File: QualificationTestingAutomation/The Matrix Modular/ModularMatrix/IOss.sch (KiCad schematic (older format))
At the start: 10 parts, among them J1 Conn_02x32_Counter_Clockwise_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, J5 Conn_02x32_Counter_Clockwise_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, J6 Banana Jack, J7 Banana Jack, J8 Banana Jack, J9 Banana Jack

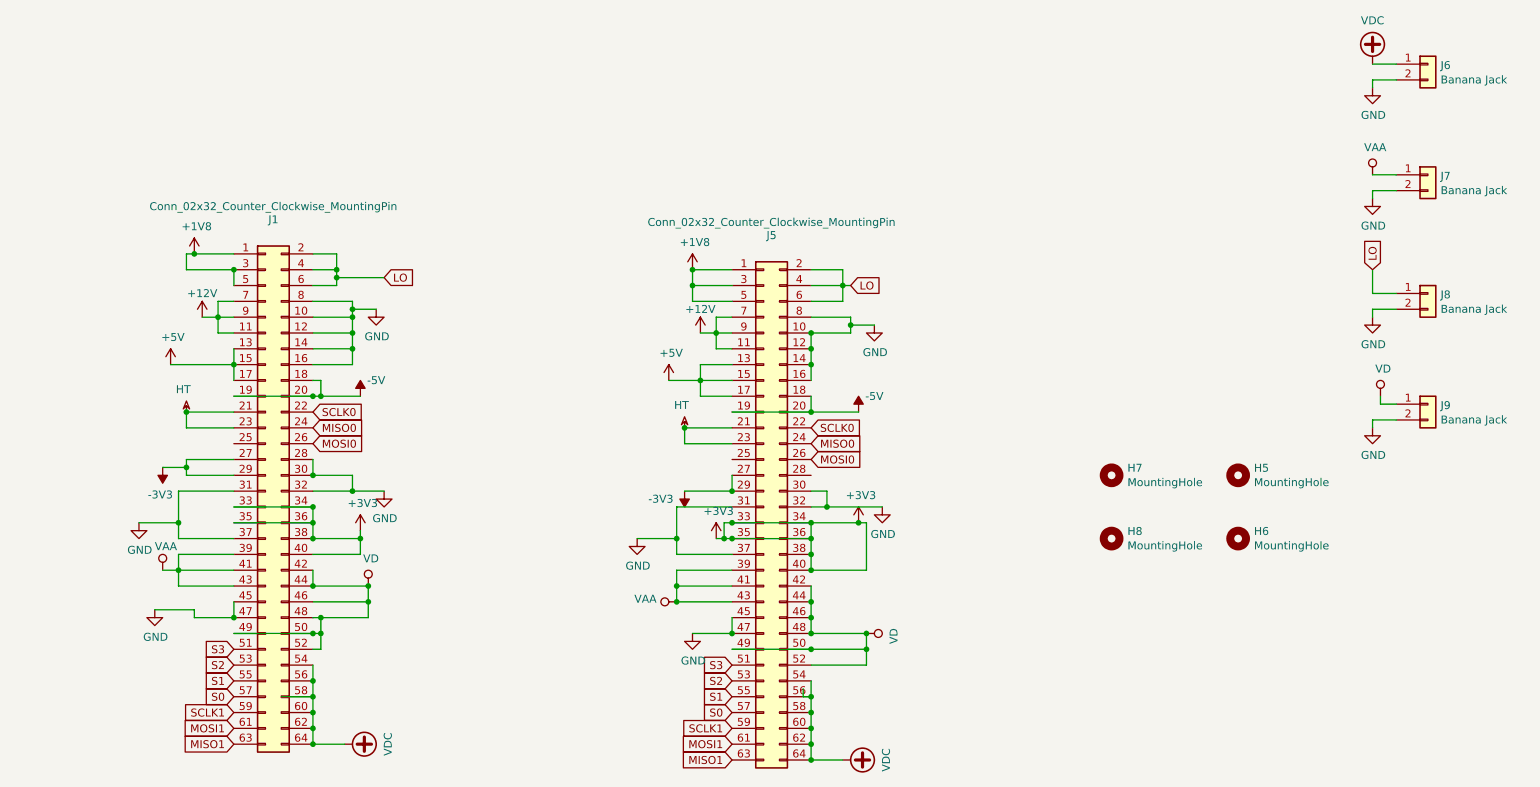
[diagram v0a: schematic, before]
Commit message: IO clean up added the 1v25 reference to Matrix Changed Some of the labels to more legible names.
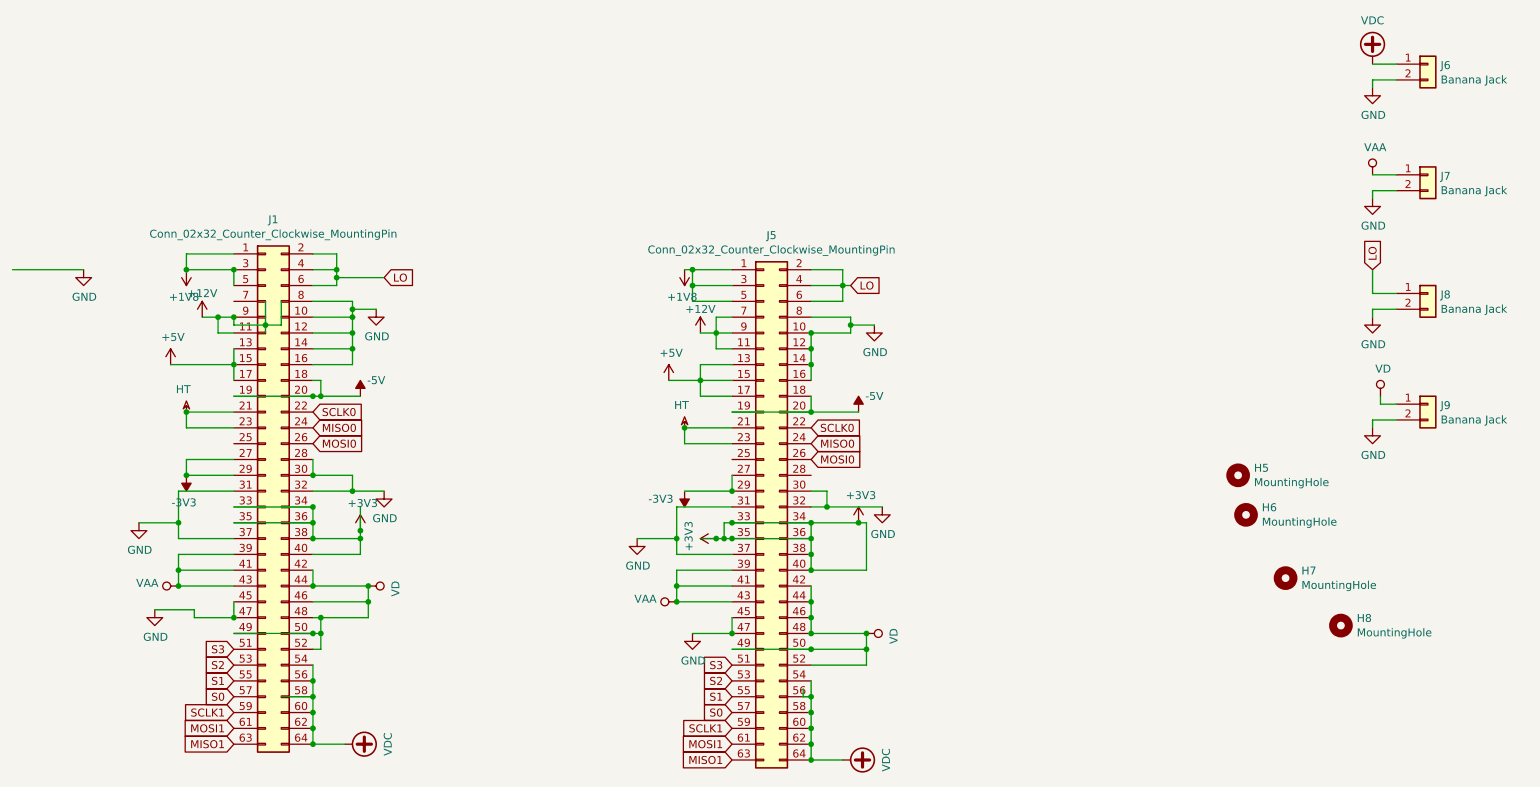
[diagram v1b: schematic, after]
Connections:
- wire segments 191 -> 195
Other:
- moved on the sheet: H6, H7, H8
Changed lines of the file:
@@
 L Mechanical:MountingHole H?
 U 1 1 5C9BCC1D
-P 9100 3900
+P 9150 3750
 AR Path="/5D942532/5C9BCC1D" Ref="H?"  Part="1"
 AR Path="/5D968A33/5C9BCC1D" Ref="H6"  Part="1"
-F 0 "H6" H 9200 3946 50  0000 L CNN
-F 1 "MountingHole" H 9200 3855 50  0000 L CNN
-F 2 "MountingHole:MountingHole_2.5mm" H 9100 3900 50  0001 C CNN
-F 3 "~" H 9100 3900 50  0001 C CNN
-	1    9100 3900
+F 0 "H6" H 9250 3796 50  0000 L CNN
+F 1 "MountingHole" H 9250 3705 50  0000 L CNN
+F 2 "MountingHole:MountingHole_2.5mm" H 9150 3750 50  0001 C CNN
+F 3 "~" H 9150 3750 50  0001 C CNN
+	1    9150 3750
 	1    0    0    -1
 $EndComp
@@
 L Mechanical:MountingHole H?
 U 1 1 5C9BCC1E
-P 8300 3500
+P 9400 4150
 AR Path="/5D942532/5C9BCC1E" Ref="H?"  Part="1"
 AR Path="/5D968A33/5C9BCC1E" Ref="H7"  Part="1"
-F 0 "H7" H 8400 3546 50  0000 L CNN
-F 1 "MountingHole" H 8400 3455 50  0000 L CNN
-F 2 "MountingHole:MountingHole_2.5mm" H 8300 3500 50  0001 C CNN
-F 3 "~" H 8300 3500 50  0001 C CNN
-	1    8300 3500
+F 0 "H7" H 9500 4196 50  0000 L CNN
+F 1 "MountingHole" H 9500 4105 50  0000 L CNN
+F 2 "MountingHole:MountingHole_2.5mm" H 9400 4150 50  0001 C CNN
+F 3 "~" H 9400 4150 50  0001 C CNN
+	1    9400 4150
 	1    0    0    -1
 $EndComp
@@
 L Mechanical:MountingHole H?
 U 1 1 5C9BCC1F
-P 8300 3900
+P 9750 4450
 AR Path="/5D942532/5C9BCC1F" Ref="H?"  Part="1"
 AR Path="/5D968A33/5C9BCC1F" Ref="H8"  Part="1"
-F 0 "H8" H 8400 3946 50  0000 L CNN
-F 1 "MountingHole" H 8400 3855 50  0000 L CNN
-F 2 "MountingHole:MountingHole_2.5mm" H 8300 3900 50  0001 C CNN
-F 3 "~" H 8300 3900 50  0001 C CNN
-	1    8300 3900
+F 0 "H8" H 9850 4496 50  0000 L CNN
+F 1 "MountingHole" H 9850 4405 50  0000 L CNN
+F 2 "MountingHole:MountingHole_2.5mm" H 9750 4450 50  0001 C CNN
+F 3 "~" H 9750 4450 50  0001 C CNN
+	1    9750 4450
 	1    0    0    -1
 $EndComp
@@
 L power:+1V8 #PWR?
 U 1 1 5DFE913D
-P 2500 2100
+P 2450 2200
 AR Path="/5D94288A/5DFE913D" Ref="#PWR?"  Part="1"
 AR Path="/5D968A33/5DFE913D" Ref="#PWR0169"  Part="1"
 AR Path="/5C90F517/5DFE913D" Ref="#PWR?"  Part="1"
-F 0 "#PWR0169" H 2500 1950 50  0001 C CNN
-F 1 "+1V8" H 2515 2273 50  0000 C CNN
-F 2 "" H 2500 2100 50  0001 C CNN
-F 3 "" H 2500 2100 50  0001 C CNN
-	1    2500 2100
-	1    0    0    -1
-$EndComp
+F 0 "#PWR0169" H 2450 2050 50  0001 C CNN
+F 1 "+1V8" H 2465 2373 50  0000 C CNN
+F 2 "" H 2450 2200 50  0001 C CNN
+F 3 "" H 2450 2200 50  0001 C CNN
+	1    2450 2200
+	-1   0    0    1
+$EndComp
+$Comp
+L power:GND #PWR0170
+U 1 1 5DFE914C
+P 1800 2200
+F 0 "#PWR0170" H 1800 1950 50  0001 C CNN
+F 1 "GND" H 1805 2027 50  0000 C CNN
+F 2 "" H 1800 2200 50  0001 C CNN
+F 3 "" H 1800 2200 50  0001 C CNN
+	1    1800 2200
+	1    0    0    -1
+$EndComp
+Wire Wire Line
+	1800 2200 1350 2200
 Wire Wire Line
 	3500 2400 3500 2450
@@
 	2450 2200 2450 2100
 Wire Wire Line
-	2450 2100 2500 2100
+	2450 2100 2750 2100
+Connection ~ 2450 2200
 $Comp
 L power:GND #PWR0171
@@
 L power:-3V3 #PWR?
 U 1 1 5DFE9176
-P 2300 3450
+P 2450 3500
 AR Path="/5D94288A/5DFE9176" Ref="#PWR?"  Part="1"
 AR Path="/5D968A33/5DFE9176" Ref="#PWR0172"  Part="1"
 AR Path="/5C90F517/5DFE9176" Ref="#PWR?"  Part="1"
-F 0 "#PWR0172" H 2300 3550 50  0001 C CNN
-F 1 "-3V3" H 2315 3623 50  0000 C CNN
-F 2 "" H 2300 3450 50  0001 C CNN
-F 3 "" H 2300 3450 50  0001 C CNN
-	1    2300 3450
+F 0 "#PWR0172" H 2450 3600 50  0001 C CNN
+F 1 "-3V3" H 2465 3673 50  0000 C CNN
+F 2 "" H 2450 3500 50  0001 C CNN
+F 3 "" H 2450 3500 50  0001 C CNN
+	1    2450 3500
 	-1   0    0    1
 $EndComp
@@
 F 3 "" H 3600 4200 50  0001 C CNN
 	1    3600 4200
-	1    0    0    -1
+	0    1    1    0
 $EndComp
 Connection ~ 3600 4200
@@
 L power:VAA #PWR0178
 U 1 1 5DFE91C4
-P 2300 4100
-F 0 "#PWR0178" H 2300 3950 50  0001 C CNN
-F 1 "VAA" H 2250 4250 50  0000 L CNN
-F 2 "" H 2300 4100 50  0001 C CNN
-F 3 "" H 2300 4100 50  0001 C CNN
-	1    2300 4100
-	1    0    0    -1
+P 2400 4200
+F 0 "#PWR0178" H 2400 4050 50  0001 C CNN
+F 1 "VAA" V 2418 4327 50  0000 L CNN
+F 2 "" H 2400 4200 50  0001 C CNN
+F 3 "" H 2400 4200 50  0001 C CNN
+	1    2400 4200
+	0    -1   -1   0
 $EndComp
 Wire Wire Line
@@
 Wire Wire Line
 	2750 3900 2400 3900
+Wire Wire Line
+	3050 2400 3050 2550
+Wire Wire Line
+	3050 2550 2950 2550
 Wire Wire Line
 	3250 2300 3400 2300
@@
 Connection ~ 3600 4300
 Wire Wire Line
-	2450 3500 2450 3450
+	2450 3500 2450 3400
 Wire Wire Line
 	2450 3400 2750 3400
+Connection ~ 2450 3500
 Wire Wire Line
 	3550 3900 3550 4000
@@
 Wire Wire Line
 	2400 4100 2400 4200
+Connection ~ 2400 4200
 Wire Wire Line
 	2400 4100 2400 4000
@@
 L power:+1V8 #PWR?
 U 1 1 5E25079F
-P 5650 2200
+P 5600 2200
 AR Path="/5D94288A/5E25079F" Ref="#PWR?"  Part="1"
 AR Path="/5D968A33/5E25079F" Ref="#PWR0182"  Part="1"
 AR Path="/5C90F517/5E25079F" Ref="#PWR?"  Part="1"
-F 0 "#PWR0182" H 5650 2050 50  0001 C CNN
-F 1 "+1V8" H 5665 2373 50  0000 C CNN
-F 2 "" H 5650 2200 50  0001 C CNN
-F 3 "" H 5650 2200 50  0001 C CNN
-	1    5650 2200
-	1    0    0    -1
+F 0 "#PWR0182" H 5600 2050 50  0001 C CNN
+F 1 "+1V8" H 5615 2373 50  0000 C CNN
+F 2 "" H 5600 2200 50  0001 C CNN
+F 3 "" H 5600 2200 50  0001 C CNN
+	1    5600 2200
+	-1   0    0    1
 $EndComp
 Wire Wire Line
@@
 Wire Wire Line
 	6650 2500 6400 2500
+Wire Wire Line
+	5600 2200 5650 2200
 $Comp
 L power:GND #PWR0183
@@
 	2450 3500 2750 3500
 Wire Wire Line
+	3550 3700 3550 3850
+Wire Wire Line
 	3250 3600 3500 3600
 Wire Wire Line
@@
 Wire Wire Line
 	3250 3400 3250 3500
+Connection ~ 3550 3850
 Wire Wire Line
 	3550 3850 3550 3900
@@
 Wire Wire Line
 	3300 4400 3600 4400
+Wire Wire Line
+	2950 2550 2950 2600
+Wire Wire Line
+	2950 2400 2950 2550
+Connection ~ 2950 2550
+Wire Wire Line
+	2750 2550 2750 2500
+Wire Wire Line
+	2750 2550 2950 2550
 Wire Wire Line
 	3550 3000 3300 3000
@@
 F 3 "" H 5800 3900 50  0001 C CNN
 	1    5800 3900
-	1    0    0    -1
+	0    -1   -1   0
 $EndComp
 Wire Wire Line
 	5850 3800 5850 3900
+Wire Wire Line
+	5800 3900 5700 3900
+Connection ~ 5800 3900
 Connection ~ 5850 3900
 Wire Wire Line
@@
 P 6100 3700
 F 0 "J5" H 6150 5417 50  0000 C CNN
-F 1 "Conn_02x32_Counter_Clockwise_MountingPin" H 6150 5500 50  0000 C CNN
+F 1 "Conn_02x32_Counter_Clockwise_MountingPin" H 6150 5326 50  0000 C CNN
 F 2 "Connector:PinHeader_2x32_P2.00mm_Vertical_Clockwise" H 6100 3700 50  0001 C CNN
 F 3 "~" H 6100 3700 50  0001 C CNN
@@
 	1    0    0    -1
 $EndComp
+Connection ~ 2750 2500
 Connection ~ 3250 5200
 Wire Wire Line
@@
 P 2950 3600
 F 0 "J1" H 3000 5317 50  0000 C CNN
-F 1 "Conn_02x32_Counter_Clockwise_MountingPin" H 3000 5400 50  0000 C CNN
+F 1 "Conn_02x32_Counter_Clockwise_MountingPin" H 3000 5226 50  0000 C CNN
 F 2 "Connector:PinHeader_2x32_P2.00mm_Vertical_Clockwise" H 2950 3600 50  0001 C CNN
 F 3 "~" H 2950 3600 50  0001 C CNN
@@
 	5900 4600 6400 4600
 Connection ~ 6400 4600
-Wire Wire Line
-	2750 2400 2650 2400
-Wire Wire Line
-	2650 2400 2650 2500
-Connection ~ 2500 2100
-Wire Wire Line
-	2500 2100 2750 2100
-Wire Wire Line
-	2450 3450 2300 3450
-Connection ~ 2450 3450
-Wire Wire Line
-	2450 3450 2450 3400
-Wire Wire Line
-	2400 4100 2300 4100
 $EndSCHEMATC
